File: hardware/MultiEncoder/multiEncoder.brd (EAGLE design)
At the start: 100 x 80 mm, 21 parts, among them J1 90325-0004, J2 90325-0004, J3 90325-0004, J4 90325-0004, U2 MCP23017T-E/SS

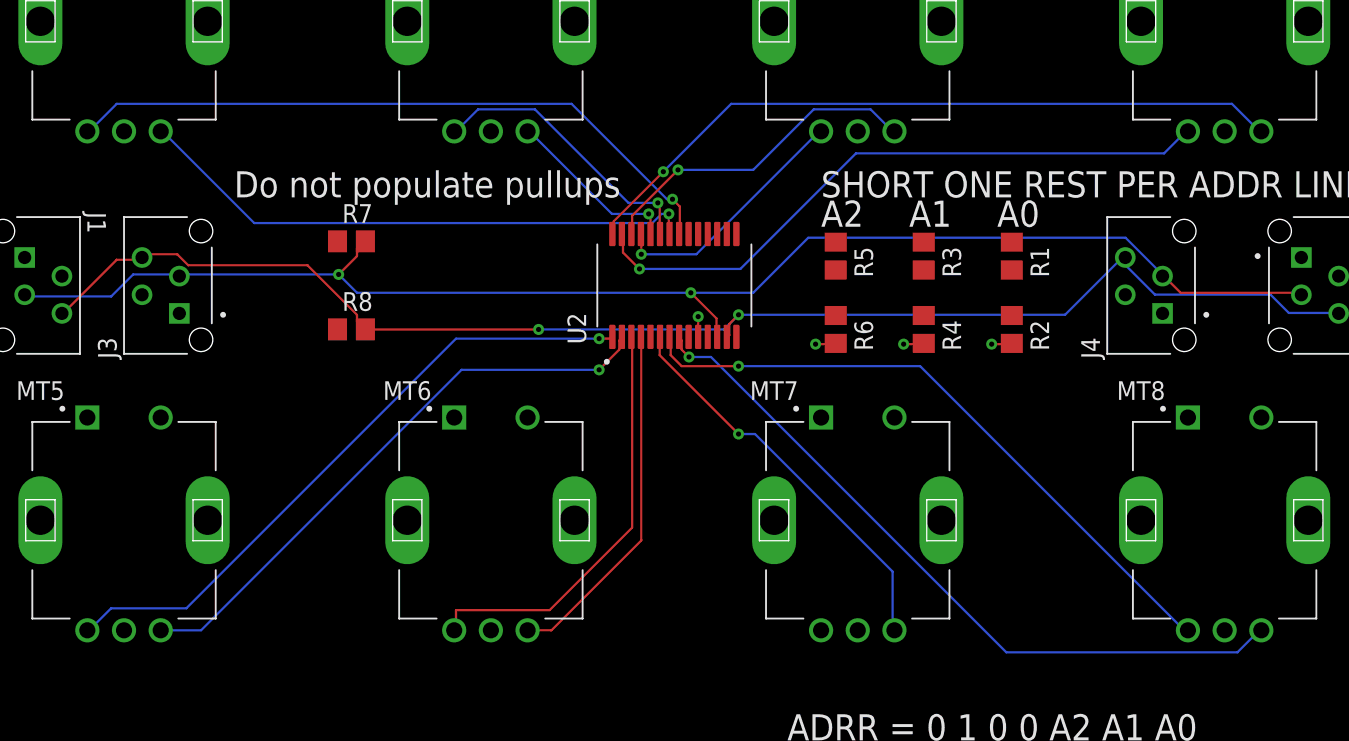
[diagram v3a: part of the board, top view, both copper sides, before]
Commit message: All signals routed, ERC and DRC passes, just need to check footprints really
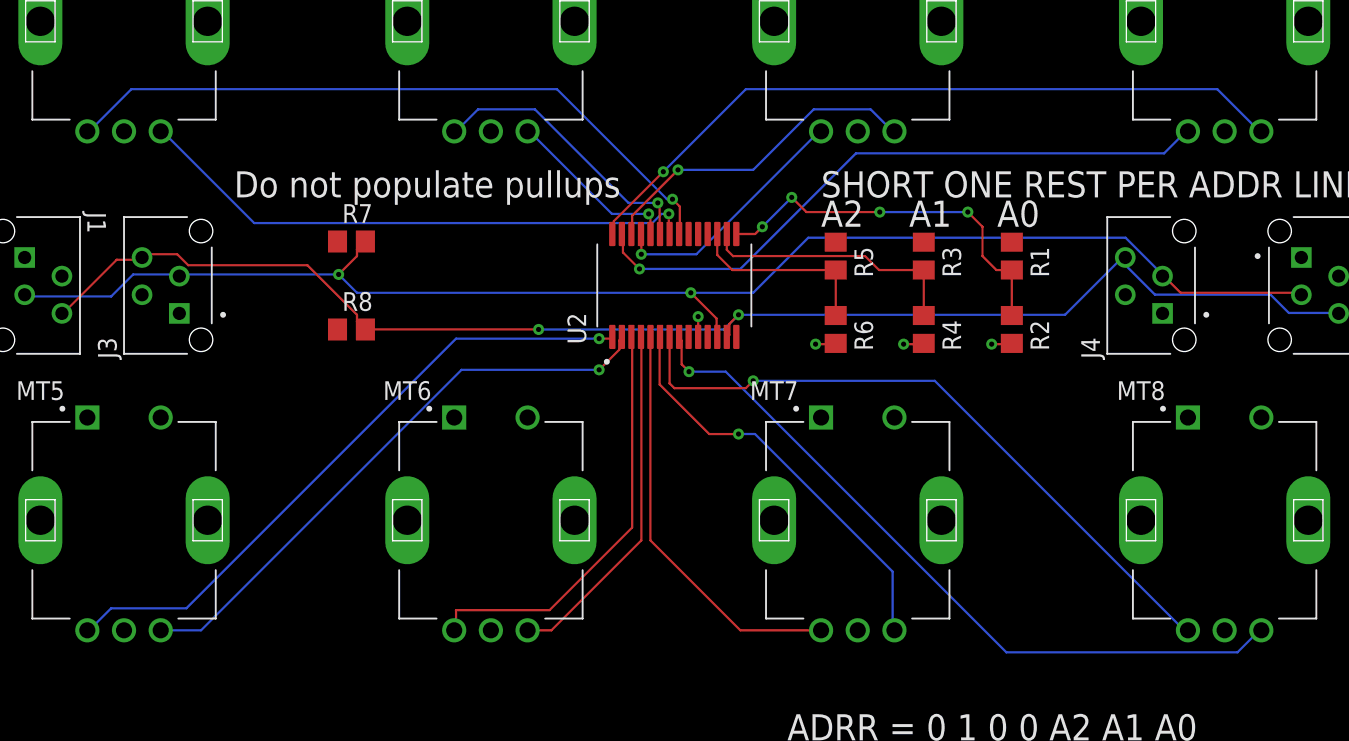
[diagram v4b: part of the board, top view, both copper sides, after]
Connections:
- removed net A7\: MT7.A
- net A7: now also MT7.A
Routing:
- net A7: track 0.00 -> 28.0 mm
- net ADR0: track 0.00 -> 26.1 mm, vias 0 -> 4
- net ADR1: track 0.00 -> 18.2 mm
- net ADR2: track 0.00 -> 13.0 mm
- net A8: track 44.3 -> 45.9 mm
- net B7: track 27.3 -> 28.5 mm
- net B4: track 49.1 -> 49.9 mm
- net A1: track 45.9 -> 46.8 mm
- net B8: track 49.6 -> 50.2 mm
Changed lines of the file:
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@@
 <param name="mtCopper" value="0.035mm 0.035mm 0.035mm 0.035mm 0.035mm 0.035mm 0.035mm 0.035mm 0.035mm 0.035mm 0.035mm 0.035mm 0.035mm 0.035mm 0.035mm 0.035mm"/>
 <param name="mtIsolate" value="1.5mm 0.15mm 0.2mm 0.15mm 0.2mm 0.15mm 0.2mm 0.15mm 0.2mm 0.15mm 0.2mm 0.15mm 0.2mm 0.15mm 0.2mm"/>
-<param name="mdWireWire" value="6mil"/>
+<param name="mdWireWire" value="10mil"/>
 <param name="mdWirePad" value="6mil"/>
 <param name="mdWireVia" value="6mil"/>
@@
 <vertex x="0" y="84"/>
 </polygon>
-<wire x1="50.975" y1="36.495" x2="52.275" y2="43.505" width="0" layer="19" extent="1-1"/>
 </signal>
 <signal name="SCL">
@@
 <wire x1="49.875" y1="45.875" x2="50.375" y2="45.375" width="0.1524" layer="1"/>
 <wire x1="49.5" y1="45.875" x2="49.875" y2="45.875" width="0.1524" layer="16"/>
-<wire x1="43" y1="52.375" x2="49.5" y2="45.875" width="0.1524" layer="16"/>
-<wire x1="12" y1="52.375" x2="43" y2="52.375" width="0.1524" layer="16"/>
-<wire x1="10.125" y1="50.5" x2="12" y2="52.375" width="0.1524" layer="16"/>
+<wire x1="42" y1="53.375" x2="49.5" y2="45.875" width="0.1524" layer="16"/>
+<wire x1="13" y1="53.375" x2="42" y2="53.375" width="0.1524" layer="16"/>
+<wire x1="10.125" y1="50.5" x2="13" y2="53.375" width="0.1524" layer="16"/>
 <wire x1="10" y1="50.5" x2="10.125" y2="50.5" width="0.1524" layer="16"/>
 <wire x1="50.375" y1="43.625" x2="50.325" y2="43.505" width="0.1524" layer="1"/>
@@
 <wire x1="45.875" y1="44.375" x2="45.875" y2="43.625" width="0.1524" layer="1"/>
 <wire x1="49.25" y1="47.75" x2="45.875" y2="44.375" width="0.1524" layer="1"/>
-<wire x1="53.875" y1="52.375" x2="49.25" y2="47.75" width="0.1524" layer="16"/>
-<wire x1="88" y1="52.375" x2="53.875" y2="52.375" width="0.1524" layer="16"/>
-<wire x1="89.875" y1="50.5" x2="88" y2="52.375" width="0.1524" layer="16"/>
+<wire x1="54.875" y1="53.375" x2="49.25" y2="47.75" width="0.1524" layer="16"/>
+<wire x1="87" y1="53.375" x2="54.875" y2="53.375" width="0.1524" layer="16"/>
+<wire x1="89.875" y1="50.5" x2="87" y2="53.375" width="0.1524" layer="16"/>
 <wire x1="90" y1="50.5" x2="89.875" y2="50.5" width="0.1524" layer="16"/>
 <wire x1="45.875" y1="43.625" x2="45.775" y2="43.505" width="0.1524" layer="1"/>
@@
 <contactref element="U2" pad="8"/>
 <wire x1="50.5" y1="36.25" x2="50.375" y2="36.375" width="0.1524" layer="1"/>
-<wire x1="50.5" y1="35.625" x2="50.5" y2="36.25" width="0.1524" layer="1"/>
-<wire x1="51" y1="35.125" x2="50.5" y2="35.625" width="0.1524" layer="1"/>
-<wire x1="52.5" y1="35.125" x2="51" y2="35.125" width="0.1524" layer="16"/>
-<wire x1="72.625" y1="15" x2="52.5" y2="35.125" width="0.1524" layer="16"/>
+<wire x1="50.5" y1="34.625" x2="50.5" y2="36.25" width="0.1524" layer="1"/>
+<wire x1="51" y1="34.125" x2="50.5" y2="34.625" width="0.1524" layer="1"/>
+<wire x1="53.5" y1="34.125" x2="51" y2="34.125" width="0.1524" layer="16"/>
+<wire x1="72.625" y1="15" x2="53.5" y2="34.125" width="0.1524" layer="16"/>
 <wire x1="88.375" y1="15" x2="72.625" y2="15" width="0.1524" layer="16"/>
 <wire x1="89.875" y1="16.5" x2="88.375" y2="15" width="0.1524" layer="16"/>
 <wire x1="90" y1="16.5" x2="89.875" y2="16.5" width="0.1524" layer="16"/>
 <wire x1="50.375" y1="36.375" x2="50.325" y2="36.495" width="0.1524" layer="1"/>
-<via x="51" y="35.125" extent="1-16" drill="0.35"/>
+<via x="51" y="34.125" extent="1-16" drill="0.35"/>
 </signal>
 <signal name="A8">
 <contactref element="MT8" pad="A"/>
 <contactref element="U2" pad="7"/>
-<wire x1="49.75" y1="35.25" x2="49.75" y2="36.375" width="0.1524" layer="1"/>
-<wire x1="50.5" y1="34.5" x2="49.75" y2="35.25" width="0.1524" layer="1"/>
-<wire x1="54.375" y1="34.5" x2="50.5" y2="34.5" width="0.1524" layer="1"/>
-<wire x1="66.75" y1="34.5" x2="54.375" y2="34.5" width="0.1524" layer="16"/>
-<wire x1="84.75" y1="16.5" x2="66.75" y2="34.5" width="0.1524" layer="16"/>
+<wire x1="67.75" y1="33.5" x2="55.375" y2="33.5" width="0.1524" layer="16"/>
+<wire x1="84.75" y1="16.5" x2="67.75" y2="33.5" width="0.1524" layer="16"/>
 <wire x1="85" y1="16.5" x2="84.75" y2="16.5" width="0.1524" layer="16"/>
-<wire x1="49.75" y1="36.375" x2="49.675" y2="36.495" width="0.1524" layer="1"/>
-<via x="54.375" y="34.5" extent="1-16" drill="0.35"/>
+<via x="55.375" y="33.5" extent="1-16" drill="0.35"/>
+<wire x1="49.675" y1="36.495" x2="49.675" y2="33.325" width="0.1524" layer="1"/>
+<wire x1="49.675" y1="33.325" x2="50" y2="33" width="0.1524" layer="1"/>
+<wire x1="50" y1="33" x2="54.875" y2="33" width="0.1524" layer="1"/>
+<wire x1="54.875" y1="33" x2="55.375" y2="33.5" width="0.1524" layer="1"/>
 </signal>
 <signal name="B7">
 <contactref element="MT7" pad="B"/>
 <contactref element="U2" pad="6"/>
-<wire x1="49" y1="35.25" x2="49" y2="36.375" width="0.1524" layer="1"/>
-<wire x1="54.375" y1="29.875" x2="49" y2="35.25" width="0.1524" layer="1"/>
+<wire x1="49" y1="33.25" x2="49" y2="36.375" width="0.1524" layer="1"/>
+<wire x1="54.375" y1="29.875" x2="52.375" y2="29.875" width="0.1524" layer="1"/>
+<wire x1="52.375" y1="29.875" x2="49" y2="33.25" width="0.1524" layer="1"/>
 <wire x1="55.5" y1="29.875" x2="54.375" y2="29.875" width="0.1524" layer="16"/>
 <wire x1="64.875" y1="20.5" x2="55.5" y2="29.875" width="0.1524" layer="16"/>
@@
 <wire x1="49" y1="36.375" x2="49.025" y2="36.495" width="0.1524" layer="1"/>
 <via x="54.375" y="29.875" extent="1-16" drill="0.35"/>
-</signal>
-<signal name="A7\">
-<contactref element="MT7" pad="A"/>
 </signal>
 <signal name="B6">
@@
 <signal name="A7">
 <contactref element="U2" pad="5"/>
+<contactref element="MT7" pad="A"/>
+<wire x1="48.375" y1="36.495" x2="48.375" y2="22.625" width="0.1524" layer="1"/>
+<wire x1="54.5" y1="16.5" x2="60" y2="16.5" width="0.1524" layer="1"/>
+<wire x1="48.375" y1="22.625" x2="54.5" y2="16.5" width="0.1524" layer="1"/>
 </signal>
 <signal name="ADR2">
@@
 <contactref element="R5" pad="2"/>
 <contactref element="R6" pad="1"/>
-<wire x1="61" y1="41.05" x2="52.925" y2="43.505" width="0" layer="19" extent="1-1"/>
-<wire x1="61" y1="37.95" x2="61" y2="41.05" width="0" layer="19" extent="1-1"/>
+<wire x1="61" y1="41.05" x2="53.95" y2="41.05" width="0.1524" layer="1"/>
+<wire x1="52.925" y1="42.075" x2="52.925" y2="43.505" width="0.1524" layer="1"/>
+<wire x1="53.95" y1="41.05" x2="52.925" y2="42.075" width="0.1524" layer="1"/>
+<wire x1="61" y1="41.05" x2="61" y2="37.95" width="0.1524" layer="1"/>
 </signal>
 <signal name="ADR1">
@@
 <contactref element="R3" pad="2"/>
 <contactref element="R4" pad="1"/>
-<wire x1="67" y1="41.05" x2="53.575" y2="43.505" width="0" layer="19" extent="1-1"/>
-<wire x1="67" y1="37.95" x2="67" y2="41.05" width="0" layer="19" extent="1-1"/>
+<wire x1="67" y1="41.05" x2="63.95" y2="41.05" width="0.1524" layer="1"/>
+<wire x1="63.95" y1="41.05" x2="63" y2="42" width="0.1524" layer="1"/>
+<wire x1="63" y1="42" x2="54" y2="42" width="0.1524" layer="1"/>
+<wire x1="54" y1="42" x2="53.575" y2="42.425" width="0.1524" layer="1"/>
+<wire x1="53.575" y1="42.425" x2="53.575" y2="43.505" width="0.1524" layer="1"/>
+<wire x1="67" y1="41.05" x2="67" y2="37.95" width="0.1524" layer="1"/>
 </signal>
 <signal name="ADR0">
@@
 <contactref element="R1" pad="2"/>
 <contactref element="R2" pad="1"/>
-<wire x1="73" y1="41.05" x2="54.225" y2="43.505" width="0" layer="19" extent="1-1"/>
-<wire x1="73" y1="37.95" x2="73" y2="41.05" width="0" layer="19" extent="1-1"/>
+<wire x1="58" y1="46" x2="59" y2="45" width="0.1524" layer="1"/>
+<via x="58" y="46" extent="1-16" drill="0.35"/>
+<wire x1="58" y1="46" x2="56" y2="44" width="0.1524" layer="16"/>
+<via x="56" y="44" extent="1-16" drill="0.35"/>
+<wire x1="56" y1="44" x2="55.505" y2="43.505" width="0.1524" layer="1"/>
+<wire x1="55.505" y1="43.505" x2="54.225" y2="43.505" width="0.1524" layer="1"/>
+<wire x1="59" y1="45" x2="64" y2="45" width="0.1524" layer="1"/>
+<via x="64" y="45" extent="1-16" drill="0.35"/>
+<wire x1="64" y1="45" x2="70" y2="45" width="0.1524" layer="16"/>
+<via x="70" y="45" extent="1-16" drill="0.35"/>
+<wire x1="70" y1="45" x2="71" y2="44" width="0.1524" layer="1"/>
+<wire x1="71" y1="44" x2="71" y2="42" width="0.1524" layer="1"/>
+<wire x1="71" y1="42" x2="71.95" y2="41.05" width="0.1524" layer="1"/>
+<wire x1="71.95" y1="41.05" x2="73" y2="41.05" width="0.1524" layer="1"/>
+<wire x1="73" y1="41.05" x2="73" y2="37.95" width="0.1524" layer="1"/>
 </signal>
 </signals>

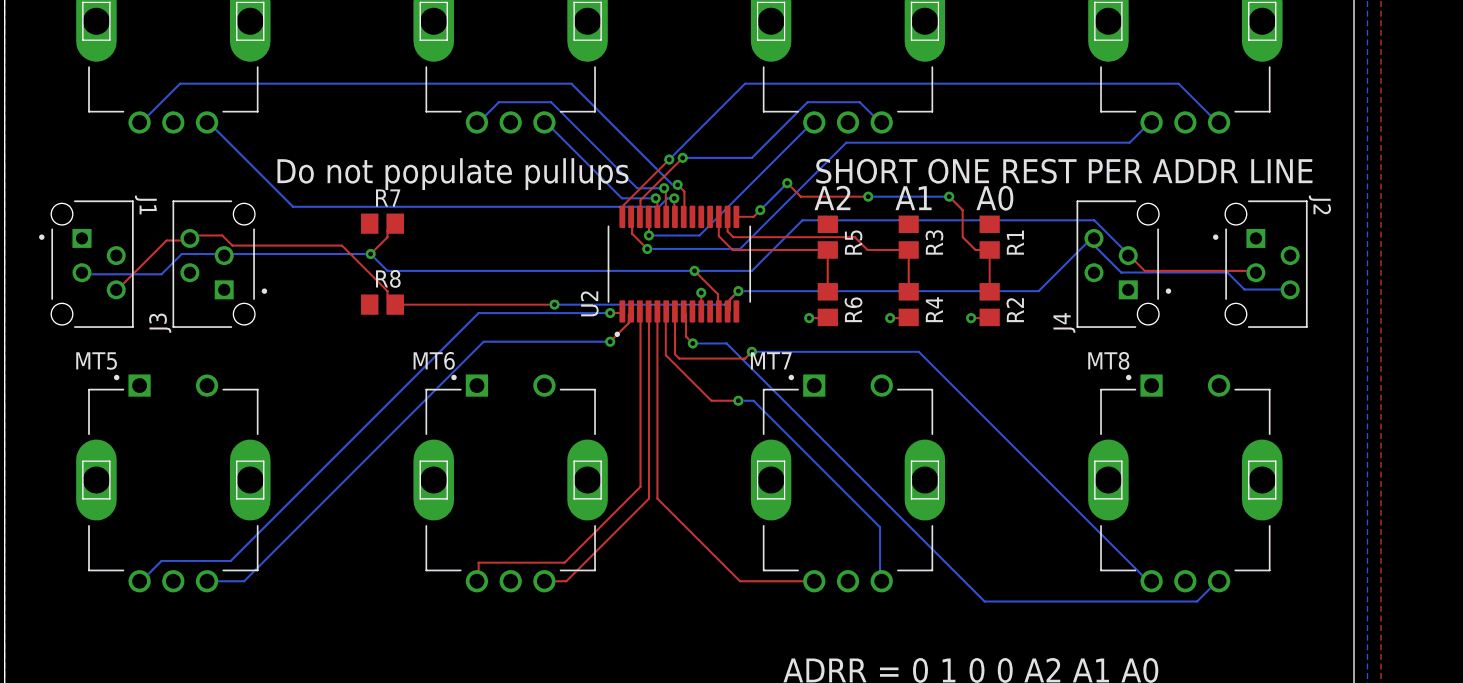
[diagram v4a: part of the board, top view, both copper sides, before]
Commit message: Switch to a dip package for the ioexpander chip, re route signals
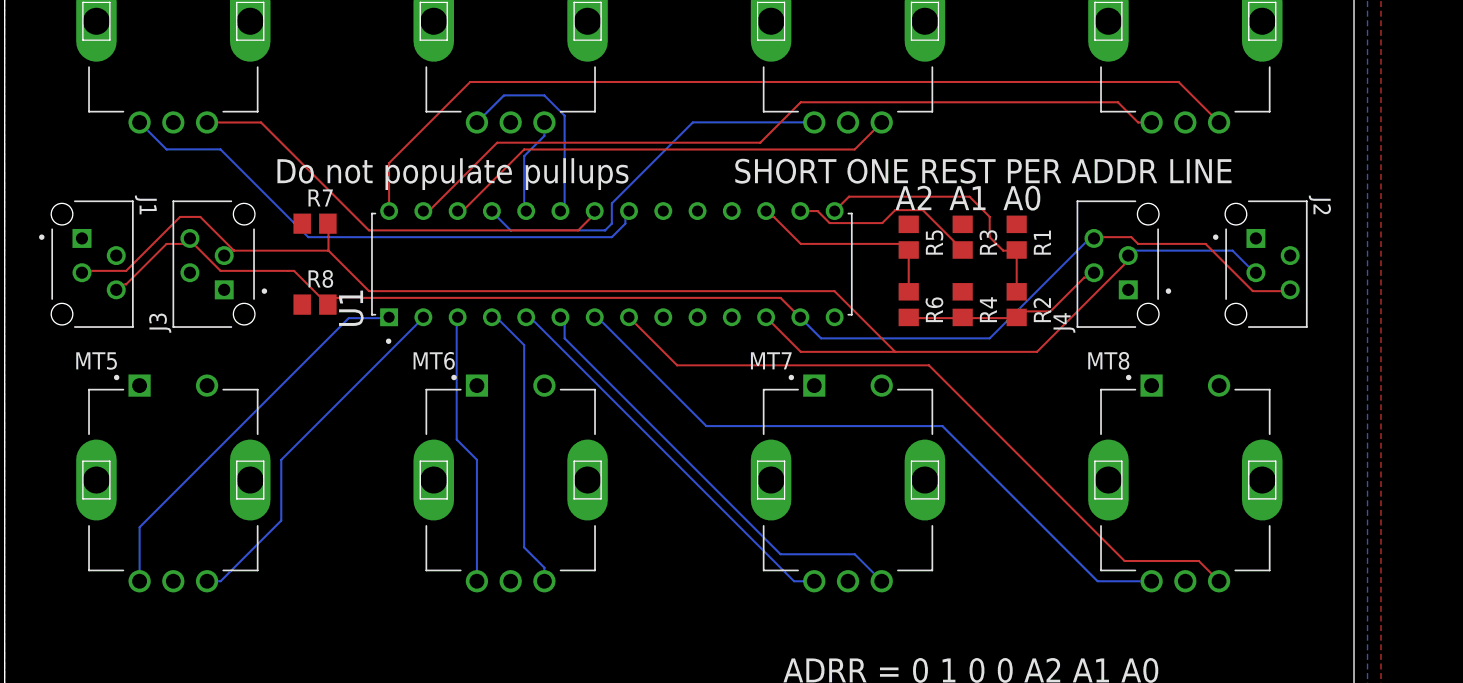
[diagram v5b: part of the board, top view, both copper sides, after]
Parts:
- removed U2: MCP23017T-E/SS, MCP23017T-E_SS:SOP65P780X200-28N
- added U1: MCP23017-E/SP, MCP23017-E_SP:DIP787W45P254L3556H508Q28
- moved R5 6.00 mm to (67.0, 42.0)
- moved R6 6.00 mm to (67.0, 37.0)
- moved R7 5.00 mm to (23.0, 43.0)
- moved R8 5.00 mm to (23.0, 37.0)
- moved R3 4.00 mm to (71.0, 42.0)
- moved R4 4.00 mm to (71.0, 37.0)
- moved R1 2.00 mm to (75.0, 42.0)
- moved R2 2.00 mm to (75.0, 37.0)
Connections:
- net A1: now also U1.21; no longer U2.21
- net A2: now also U1.23; no longer U2.23
- net A3: now also U1.25; no longer U2.25
- net A4: now also U1.27; no longer U2.27
- net A5: now also U1.1; no longer U2.1
- net A6: now also U1.3; no longer U2.3
- net A7: now also U1.5; no longer U2.5
- net A8: now also U1.7; no longer U2.7
- net ADR0: now also U1.15; no longer U2.15
- net ADR1: now also U1.16; no longer U2.16
- net ADR2: now also U1.17; no longer U2.17
- net B1: now also U1.22; no longer U2.22
- net B2: now also U1.24; no longer U2.24
- net B3: now also U1.26; no longer U2.26
- net B4: now also U1.28; no longer U2.28
- net B5: now also U1.2; no longer U2.2
- net B6: now also U1.4; no longer U2.4
- net B7: now also U1.6; no longer U2.6
- net B8: now also U1.8; no longer U2.8
- net GND: now also U1.10; no longer U2.10
- net SCL: now also U1.12; no longer U2.12
- net SDA: now also U1.13; no longer U2.13
- net VCC: now also U1.18, U1.9; no longer U2.18, U2.9
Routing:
- net B4: track 49.9 -> 69.1 mm, vias 1 -> 0
- net A5: track 44.1 -> 28.9 mm, vias 1 -> 0
- net A4: track 44.2 -> 57.9 mm, vias 1 -> 0
- net B5: track 40.1 -> 26.8 mm, vias 1 -> 0
- net SCL: track 98.5 -> 110.7 mm, vias 2 -> 0
- net B3: track 22.8 -> 34.4 mm, vias 1 -> 0
- net A3: track 17.1 -> 28.7 mm, vias 1 -> 0
- net GND: track 5.65 -> 15.6 mm, vias 4 -> 0
- net A6: track 28.8 -> 20.2 mm
- net ADR0: track 26.1 -> 19.5 mm, vias 4 -> 0
- net B1: track 38.9 -> 32.7 mm, vias 1 -> 0
- net A1: track 46.8 -> 40.9 mm, vias 1 -> 0
- net B2: track 12.0 -> 7.28 mm, vias 1 -> 0
- net B7: track 28.5 -> 32.8 mm, vias 1 -> 0
- net ADR1: track 18.2 -> 14.0 mm
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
